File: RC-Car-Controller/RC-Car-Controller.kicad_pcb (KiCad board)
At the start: 4 copper layers, 138 x 77 mm, 101 parts, among them J1 Conn_01x02, J2 RF_IF, J3 Conn_01x08_Pin, J5 MCU_IF, J6 ANT_IF, J7 2171790001, Q1 DMG2301L, SW1 SW_Push, SW2 1825027-8, SW3 SW_SPDT, SW4 1825027-8, U1 TPS62132, U10 STC3100IST, U2 USBLC6-2SC6, U4 STM32H743VGTx, U8 BQ25303JRTER, Y1 Crystal

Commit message: Finished Controller PCB Pre-Review
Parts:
- removed D6, D7: ESD9B5.0ST5G, Diode_SMD:D_SOD-923
- added ?: , , F.Cu at (203.6, 97.5)
- added ?: , , F.Cu at (203.5, 53.7)
- added ?: , , F.Cu at (95.9, 53.7)
- added C26: DNP, Capacitor_SMD:C_0603_1608Metric, F.Cu at (192.4, 54.6)
- added C28: DNP, Capacitor_SMD:C_0603_1608Metric, F.Cu at (192.4, 50.0)
- added FB1: FerriteBead, Capacitor_SMD:C_0603_1608Metric, F.Cu at (183.9, 48.6)
- added R3: 60ohm, Resistor_SMD:R_0603_1608Metric, F.Cu at (127.1, 46.8)
- added R35: 10k, Capacitor_SMD:C_0603_1608Metric, F.Cu at (197.4, 70.2)
- added R36: 10k, Capacitor_SMD:C_0603_1608Metric, F.Cu at (197.4, 65.3)
- added R37: 10k, Capacitor_SMD:C_0603_1608Metric, F.Cu at (197.4, 66.9)
- added R38: 0ohm, Resistor_SMD:R_0603_1608Metric, F.Cu at (191.6, 52.3)
- added R39: 10k, Capacitor_SMD:C_0603_1608Metric, F.Cu at (197.4, 68.6)
- added REF**: MountingHole_3.2mm_M3, MountingHole:MountingHole_3.2mm_M3, F.Cu at (96.0, 97.7)
- added REF**: Overtime_Large, _LOGOS:Overtime_Large, F.Cu at (115.4, 111.8)
- added REF**: MountingHole_3.2mm_M3, MountingHole:MountingHole_3.2mm_M3, F.Cu at (95.9, 53.7)
- added REF**: MountingHole_3.2mm_M3, MountingHole:MountingHole_3.2mm_M3, F.Cu at (203.6, 97.7)
- added REF**: MountingHole_3.2mm_M3, MountingHole:MountingHole_3.2mm_M3, F.Cu at (203.5, 53.7)
- added TP1: TestPoint, Connector_PinHeader_2.54mm:PinHeader_1x02_P2.54mm_Vertical, F.Cu at (100.2, 59.7)
- added TP2: TestPoint, Connector_PinHeader_2.54mm:PinHeader_1x02_P2.54mm_Vertical, F.Cu at (100.2, 70.7)
- added TP3: TestPoint, Connector_PinHeader_2.54mm:PinHeader_1x02_P2.54mm_Vertical, F.Cu at (100.2, 67.1)
- added TP4: TestPoint, Connector_PinHeader_2.54mm:PinHeader_1x02_P2.54mm_Vertical, F.Cu at (182.2, 94.4)
- added TP5: TestPoint, Connector_PinHeader_2.54mm:PinHeader_1x02_P2.54mm_Vertical, F.Cu at (100.2, 63.4)
- added TP6: TestPoint, Connector_PinHeader_2.54mm:PinHeader_1x02_P2.54mm_Vertical, F.Cu at (185.9, 94.4)
- D3: value ESD9B5.0ST5G -> LED; footprint Diode_SMD:D_SOD-923 -> LED_THT:LED_D5.0mm
- R1: renamed from R7; value 1.5kohm -> 220ohm
- R15: renamed from R1; footprint Resistor_SMD:R_0603_1608Metric -> Resistor_SMD:R_0805_2012Metric
- R8: renamed from R9; value 1kohm -> 220ohm
- moved D3 108.9 mm to (132.6, 47.0), turned to 180 degrees
- moved SW1 70.4 mm to (180.7, 78.2)
- moved J4 4.43 mm to (191.3, 61.8)
- moved C29 1.26 mm to (183.9, 50.3), turned to 180 degrees
- moved C27 1.08 mm to (183.9, 51.9), turned to 180 degrees
- moved R48 0.32 mm to (210.8, 118.2)
- moved J2 0.18 mm to (167.5, 46.1)
- renumbered C17 to C10, C3 to C11, C4 to C12, C5 to C13, C6 to C14, C7 to C15, C8 to C16, C9 to C17, C10 to C18, C11 to C19, C12 to C20, C13 to C21, C21 to C22, C26 to C23, C29 to C24, C28 to C25, C25 to C27, C27 to C29, C14 to C3, C23 to C30, C24 to C31, C20 to C4, C19 to C5, C18 to C6, C15 to C7, C22 to C8, C16 to C9, J7 to J2, J5 to J3, J2 to J4, J6 to J5, J3 to J6, L2 to L1, L1 to L2, R14 to R10, R18 to R11, R15 to R12, R22 to R13, R4 to R14, R11 to R16, R12 to R17, R25 to R18, R5 to R19, R8 to R2, R6 to R20, R19 to R21, R20 to R22, R42 to R23, R41 to R24, R39 to R25, R38 to R26, R37 to R27, R36 to R28, R40 to R29, R35 to R30, R34 to R31, R33 to R32, R32 to R33, R27 to R34, R24 to R4, R31 to R40, R30 to R41, R29 to R42, R28 to R43, R26 to R44, R17 to R45, R16 to R46, R2 to R47, R3 to R48, R23 to R5, R21 to R6, R10 to R7, R13 to R9, SW3 to SW2, SW4 to SW3, SW2 to SW4, U2 to U1, U8 to U2, U1 to U3, U10 to U4, U4 to U5, U3 to U6
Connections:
- net /MCU/RF_BUSY renamed /RF/BUSY
- C27 pad 1: +3V3 -> VDD_FEM
- C29 pad 1: +3V3 -> VDD_FEM
- D3 pad 2: +3V3 -> Net-(D3-A)
- U5 pad 72: unconnected-(U4-PA13-Pad72) -> /Connectors/SWDIO
- U5 pad 77: /Connectors/SWDIO -> unconnected-(U5-PA15-Pad77)
- U5 pad 81: unconnected-(U4-PD0-Pad81) -> /MCU/RF_RESET
- U6 pad 4: +3V3 -> VDD_FEM
- U6 pad 40: /Connectors/RF_ANT -> Net-(U6-ANT_WIFI)
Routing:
- net /MCU/RF_RESET: track 3.06 -> 33.1 mm, vias 0 -> 2
- net /Connectors/NRST: track 40.7 -> 69.2 mm
- net /Inputs/Button_R: track 103.7 -> 89.2 mm
- net GNDA: track 36.1 -> 48.6 mm, vias 95 -> 128
- net +3V3: track 37.0 -> 47.5 mm, vias 37 -> 39
- net /Connectors/RF_TCK: track 6.11 -> 14.5 mm
- net VDD_USB: track 111.8 -> 118.0 mm
- net /Connectors/RF_ANT: track 12.4 -> 6.16 mm
- net VDD_FEM: track 0.00 -> 6.21 mm
- net Net-(U6-ANT_WIFI): track 0.00 -> 5.33 mm
- net /Connectors/RF_TDI: track 8.30 -> 13.6 mm, vias 0 -> 1
- net /Connectors/RF_TDO: track 8.08 -> 11.8 mm
- net Net-(D3-A): track 0.00 -> 3.34 mm
- net /Inputs/Slider_R: track 98.0 -> 95.2 mm
- net /Connectors/SWDIO: track 21.8 -> 19.2 mm
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- added copper zone on In2.Cu, net GNDA
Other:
- board size 138 x 77 mm -> 138.8 x 77 mm
- board text added: "!! 50 OHM IMPEDENCE >>"
- board text added: "3V3"
- board text added: "3V3 TMS TCK"
- board text added: "BAT"
- board text added: "GND"
- board text added: "GND RST TDI TDO"
- board text added: "OVERTIME GAMES"
- board text added: "ROVERTIME CONTROLLER"
- board text added: "RX DIO GND"
- board text added: "TX CLK RST 3V3"
- board text added: "USB"
- board text added: "V1"

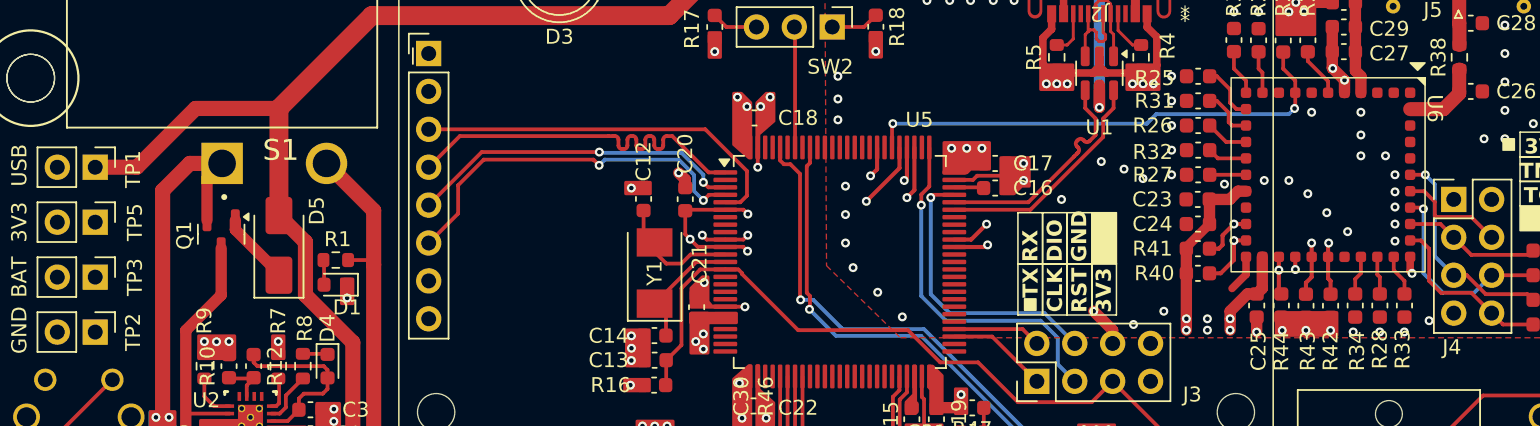
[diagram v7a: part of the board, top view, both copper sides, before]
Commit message: Laid out 3V3 section of Tank PCB
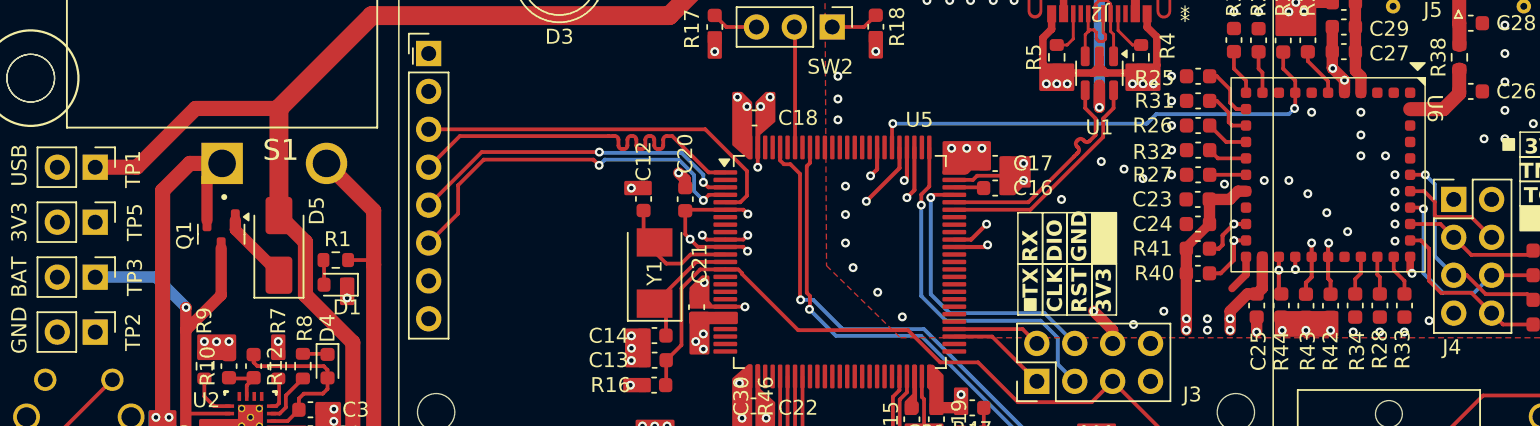
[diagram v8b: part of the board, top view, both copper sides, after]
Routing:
- net VDD_BATT: track 38.0 -> 46.5 mm, vias 0 -> 1
- added copper zone on In1.Cu, net +3V3
- removed copper zone on In2.Cu, net +3V3
- removed copper zone on In1.Cu, net GNDA
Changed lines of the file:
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@@
 		(tags "Through hole pin header THT 1x02 2.54mm single row")
 		(property "Reference" "TP6"
-			(at 0 -2.794 360)
+			(at 0 -2.794 0)
 			(layer "F.SilkS")
 			(effects
@@
 		)
 		(property "Value" "TestPoint"
-			(at 0 4.87 360)
+			(at 0 4.87 0)
 			(layer "F.Fab")
 			(effects
@@
 		(tags "capacitor")
 		(property "Reference" "R35"
-			(at -2.921 0 360)
+			(at -2.921 0 0)
 			(layer "F.SilkS")
 			(effects
@@
 		)
 		(property "Value" "10k"
-			(at 0 1.43 360)
+			(at 0 1.43 0)
 			(layer "F.Fab")
 			(effects
@@
 		)
 		(fp_text user "${REFERENCE}"
-			(at 0 0 360)
+			(at 0 0 0)
 			(layer "F.Fab")
 			(effects
@@
 		(tags "capacitor")
 		(property "Reference" "R37"
-			(at -2.921 0 360)
+			(at -2.921 0 0)
 			(layer "F.SilkS")
 			(effects
@@
 		)
 		(property "Value" "10k"
-			(at 0 1.43 360)
+			(at 0 1.43 0)
 			(layer "F.Fab")
 			(effects
@@
 		)
 		(fp_text user "${REFERENCE}"
-			(at 0 0 360)
+			(at 0 0 0)
 			(layer "F.Fab")
 			(effects
@@
 		(tags "capacitor")
 		(property "Reference" "R39"
-			(at -2.921 0 360)
+			(at -2.921 0 0)
 			(layer "F.SilkS")
 			(effects
@@
 		)
 		(property "Value" "10k"
-			(at 0 1.43 360)
+			(at 0 1.43 0)
 			(layer "F.Fab")
 			(effects
@@
 		)
 		(fp_text user "${REFERENCE}"
-			(at 0 0 360)
+			(at 0 0 0)
 			(layer "F.Fab")
 			(effects
@@
 		(tags "LED")
 		(property "Reference" "D3"
-			(at 1.27 -3.96 360)
+			(at 1.27 -3.96 0)
 			(layer "F.SilkS")
 			(effects
@@
 		)
 		(property "Value" "LED"
-			(at 1.27 3.96 360)
+			(at 1.27 3.96 0)
 			(layer "F.Fab")
 			(effects
@@
 		)
 		(property "Footprint" "LED_THT:LED_D5.0mm"
-			(at 0 0 360)
+			(at 0 0 0)
 			(layer "F.Fab")
 			(hide yes)
@@
 		)
 		(property "Datasheet" ""
-			(at 0 0 360)
+			(at 0 0 0)
 			(layer "F.Fab")
 			(hide yes)
@@
 		)
 		(property "Description" "Light emitting diode"
-			(at 0 0 360)
+			(at 0 0 0)
 			(layer "F.Fab")
 			(hide yes)
@@
 		)
 		(fp_text user "${REFERENCE}"
-			(at 1.27 0 360)
+			(at 1.27 0 0)
 			(layer "F.Fab")
 			(effects
@@
 		(tags "Through hole pin header THT 1x02 2.54mm single row")
 		(property "Reference" "TP4"
-			(at -0.127 -2.662 360)
+			(at -0.127 -2.662 0)
 			(layer "F.SilkS")
 			(effects
@@
 		)
 		(property "Value" "TestPoint"
-			(at 0 4.87 360)
+			(at 0 4.87 0)
 			(layer "F.Fab")
 			(effects
@@
 		(at 182.841 60.198 -90)
 		(property "Reference" "U6"
-			(at -4.445 -7.151 270)
+			(at -4.445 -7.151 -90)
 			(unlocked yes)
 			(layer "F.SilkS")
@@
 		(tags "capacitor")
 		(property "Reference" "R36"
-			(at -2.921 0 360)
+			(at -2.921 0 0)
 			(layer "F.SilkS")
 			(effects
@@
 		)
 		(property "Value" "10k"
-			(at 0 1.43 360)
+			(at 0 1.43 0)
 			(layer "F.Fab")
 			(effects
@@
 		)
 		(fp_text user "${REFERENCE}"
-			(at 0 0 360)
+			(at 0 0 0)
 			(layer "F.Fab")
 			(effects
@@
 		(tags "capacitor")
 		(property "Reference" "C27"
-			(at -3.048 -0.127 360)
+			(at -3.048 -0.127 0)
 			(layer "F.SilkS")
 			(effects
@@
 		)
 		(property "Value" "10uF/10V"
-			(at 0 1.43 360)
+			(at 0 1.43 0)
 			(layer "F.Fab")
 			(effects
@@
 		)
 		(fp_text user "${REFERENCE}"
-			(at 0 0 360)
+			(at 0 0 0)
 			(layer "F.Fab")
 			(effects
@@
 		)
 		(fp_text user "${REFERENCE}"
-			(at 0 1.27 360)
+			(at 0 1.27 0)
 			(layer "F.Fab")
 			(effects
@@
 		)
 		(fp_text user "${REFERENCE}"
-			(at 0 1.27 360)
+			(at 0 1.27 0)
 			(layer "F.Fab")
 			(effects
@@
 		(tags "capacitor")
 		(property "Reference" "C29"
-			(at -3.048 -0.127 360)
+			(at -3.048 -0.127 0)
 			(layer "F.SilkS")
 			(effects
@@
 		)
 		(property "Value" "100nF/10V"
-			(at 0 1.43 360)
+			(at 0 1.43 0)
 			(layer "F.Fab")
 			(effects
@@
 		)
 		(fp_text user "${REFERENCE}"
-			(at 0 0 360)
+			(at 0 0 0)
 			(layer "F.Fab")
 			(effects
@@
 		)
 		(fp_text user "${REFERENCE}"
-			(at 0 1.27 360)
+			(at 0 1.27 0)
 			(layer "F.Fab")
 			(effects
@@
 		)
 		(fp_text user "${REFERENCE}"
-			(at 0 1.27 360)
+			(at 0 1.27 0)
 			(layer "F.Fab")
 			(effects
@@
 	)
 	(segment
+		(start 106.280172 69.106828)
+		(end 106.299 69.088)
+		(width 0.762)
+		(layer "F.Cu")
+		(net 11)
+	)
+	(segment
 		(start 106.463 81.661)
 		(end 107.079502 81.044498)
@@
 	)
 	(segment
+		(start 106.280172 70.630828)
+		(end 106.280172 69.106828)
+		(width 0.762)
+		(layer "F.Cu")
+		(net 11)
+	)
+	(via
+		(at 106.299 69.088)
+		(size 0.6)
+		(drill 0.3)
+		(layers "F.Cu" "B.Cu")
+		(net 11)
+	)
+	(segment
 		(start 101.859 81.783)
 		(end 101.981 81.661)
@@
 	)
 	(segment
+		(start 104.267 67.056)
+		(end 100.208 67.056)
+		(width 0.762)
+		(layer "B.Cu")
+		(net 11)
+	)
+	(segment
+		(start 106.299 69.088)
+		(end 104.267 67.056)
+		(width 0.762)
+		(layer "B.Cu")
+		(net 11)
+	)
+	(segment
 		(start 115.5445 67.564)
 		(end 115.5445 65.9505)
@@
 	)
 	(zone
-		(net 3)
-		(net_name "GNDA")
+		(net 1)
+		(net_name "+3V3")
 		(layer "In1.Cu")
 		(hatch edge 0.5)
@@
 		(polygon
 			(pts
-				(xy 82.804 97.663) (xy 216.789 97.663) (xy 216.789 44.196) (xy 82.804 44.196)
+				(xy 82.677 118.618) (xy 216.789 118.618) (xy 216.789 44.196) (xy 82.804 44.196)
 			)
 		)
@@
 		(net_name "GNDA")
 		(layer "In2.Cu")
-		(name "RF_WAVEGUIDE")
-		(hatch edge 0.5)
-		(priority 3)
-		(connect_pads
-			(clearance 0)
-		)
-		(min_thickness 0.25)
-		(filled_areas_thickness no)
-		(fill yes
-			(thermal_gap 0.5)
-			(thermal_bridge_width 0.5)
-		)
-		(polygon
-			(pts
-				(xy 185.547 58.42) (xy 185.547 44.196) (xy 199.136 44.196) (xy 199.136 58.42)
-			)
-		)
-	)
-	(zone
-		(net 1)
-		(net_name "+3V3")
-		(layer "In2.Cu")
 		(hatch edge 0.5)
